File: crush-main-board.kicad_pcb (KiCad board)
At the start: 2 copper layers, 101.6 x 120.6 mm, 47 parts, among them J1 4x4_Header, J10 3x3 Header, J11 3x3 Header, J12 3x2 Header, J13 3x4_Header, J14 3x4_Header, J15 2157601008, J16 Conn_01x02, J17 Conn_01x02, J2 4x4_Header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

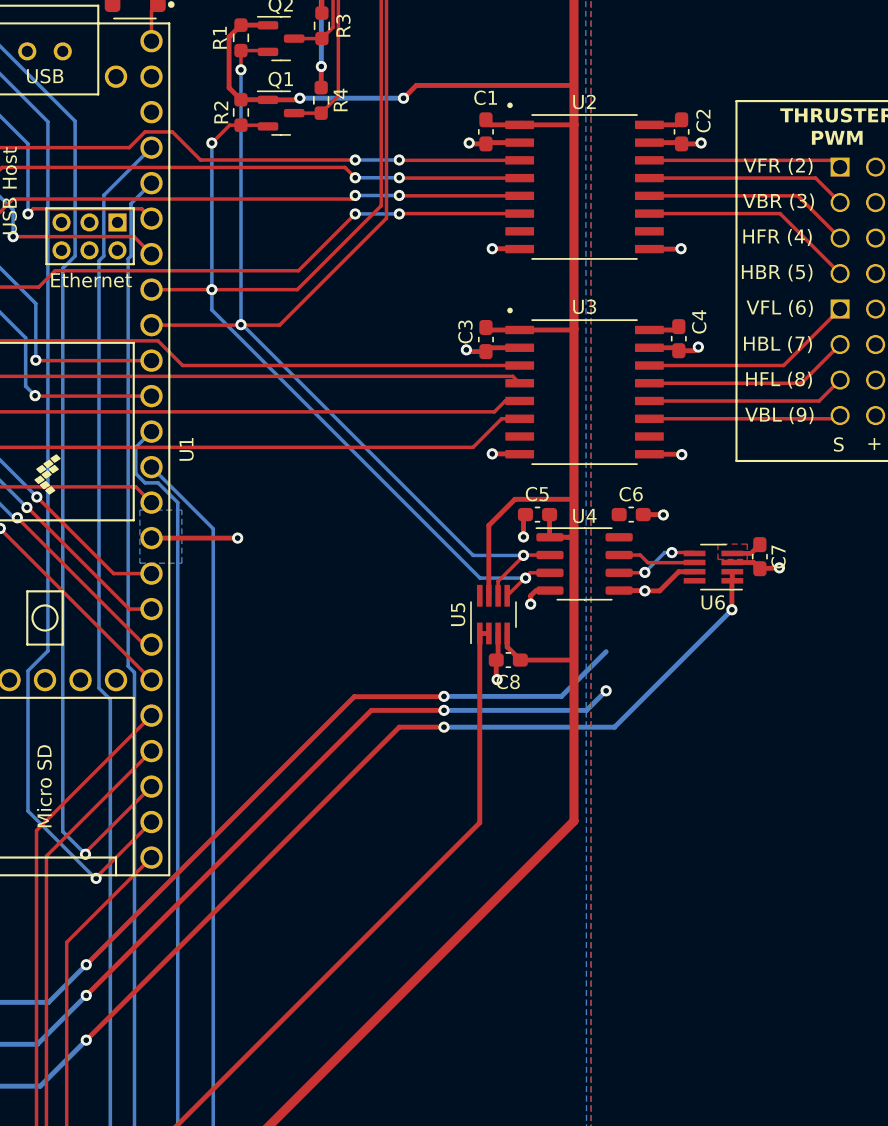
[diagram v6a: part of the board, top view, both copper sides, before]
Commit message: use 0805 footprints for decoupling capacitors
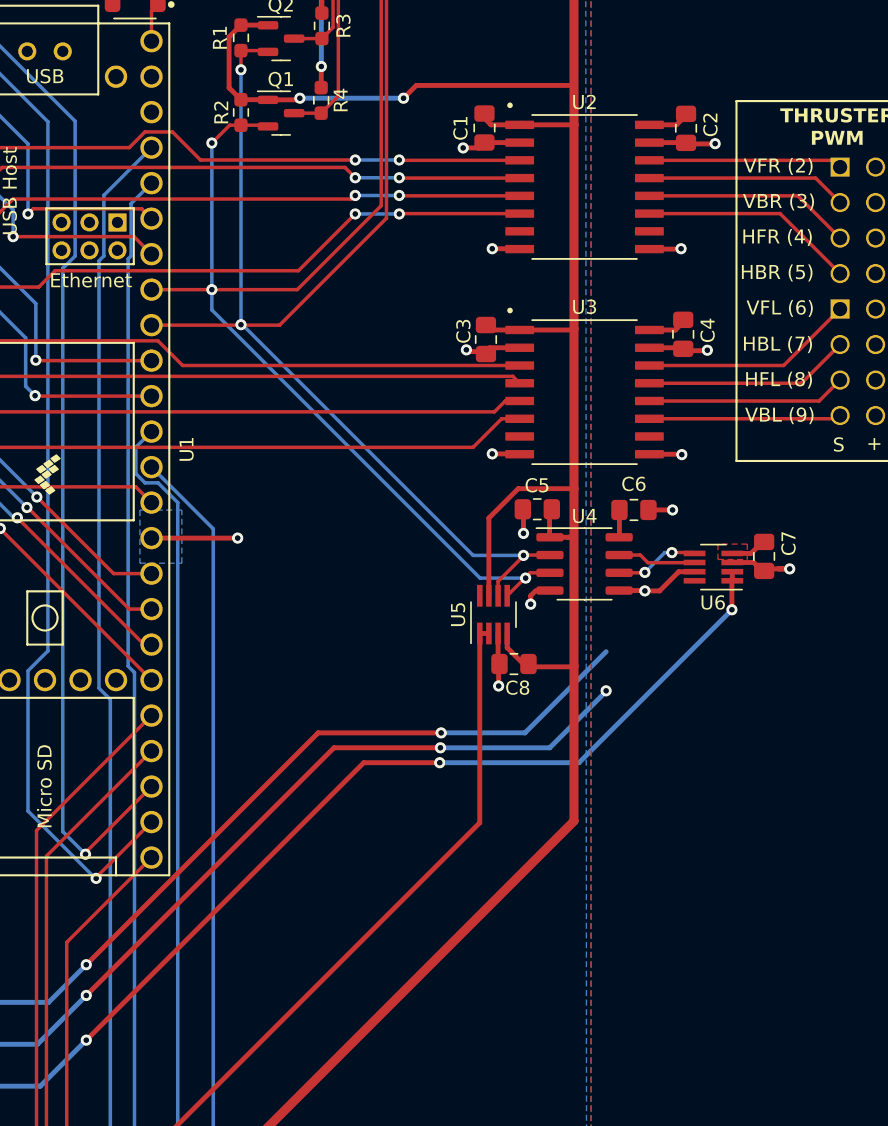
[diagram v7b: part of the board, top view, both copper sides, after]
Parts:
- C1, C2, C3, C4, C5, C6, C7, C8: footprint Capacitor_SMD:C_0603_1608Metric_Pad1.08x0.95mm_HandSolder -> Capacitor_SMD:C_0805_2012Metric_Pad1.18x1.45mm_HandSolder
- moved C8 0.49 mm to (84.2, 71.9)
- moved C4 0.44 mm to (96.3, 48.3)
- moved C2 0.41 mm to (96.5, 33.5)
- moved C6 0.38 mm to (92.8, 60.9)
- moved C5 0.38 mm to (85.9, 60.8)
- moved C7 0.31 mm to (102.1, 64.2)
- moved C1 0.29 mm to (82.1, 33.5)
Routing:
- net GND_T: track 101.8 -> 104.8 mm
- net +3V3_T: track 85.1 -> 87.2 mm
- net +3V3: track 333.0 -> 334.6 mm
